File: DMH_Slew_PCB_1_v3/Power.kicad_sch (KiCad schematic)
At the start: 13 parts, among them J0 Conn_01x01, J100 IDC_02x08, J200 IDC_02x05, U10 LM4040LP-10, U11 LM4040LP-10

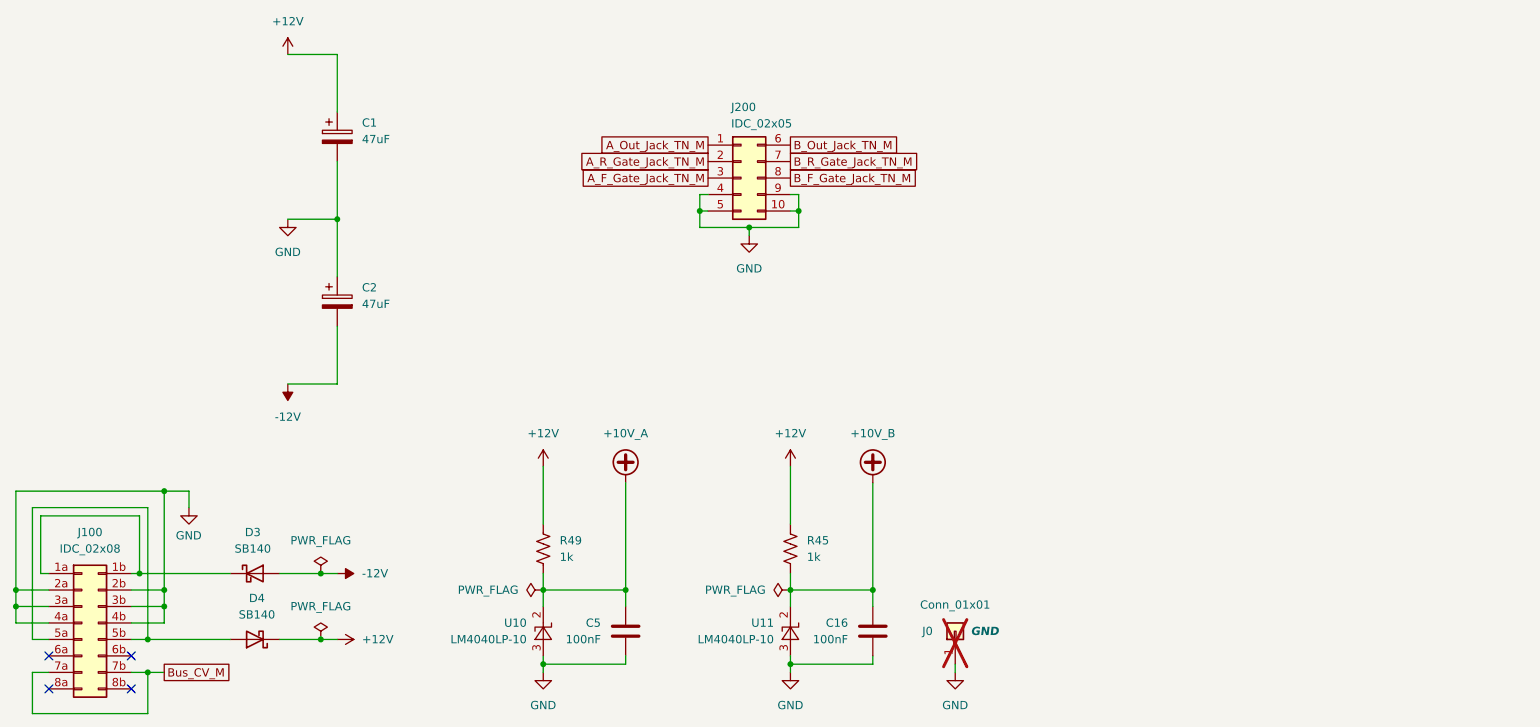
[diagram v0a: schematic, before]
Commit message: Redesigned Main PCB
and regenerated Gerbers
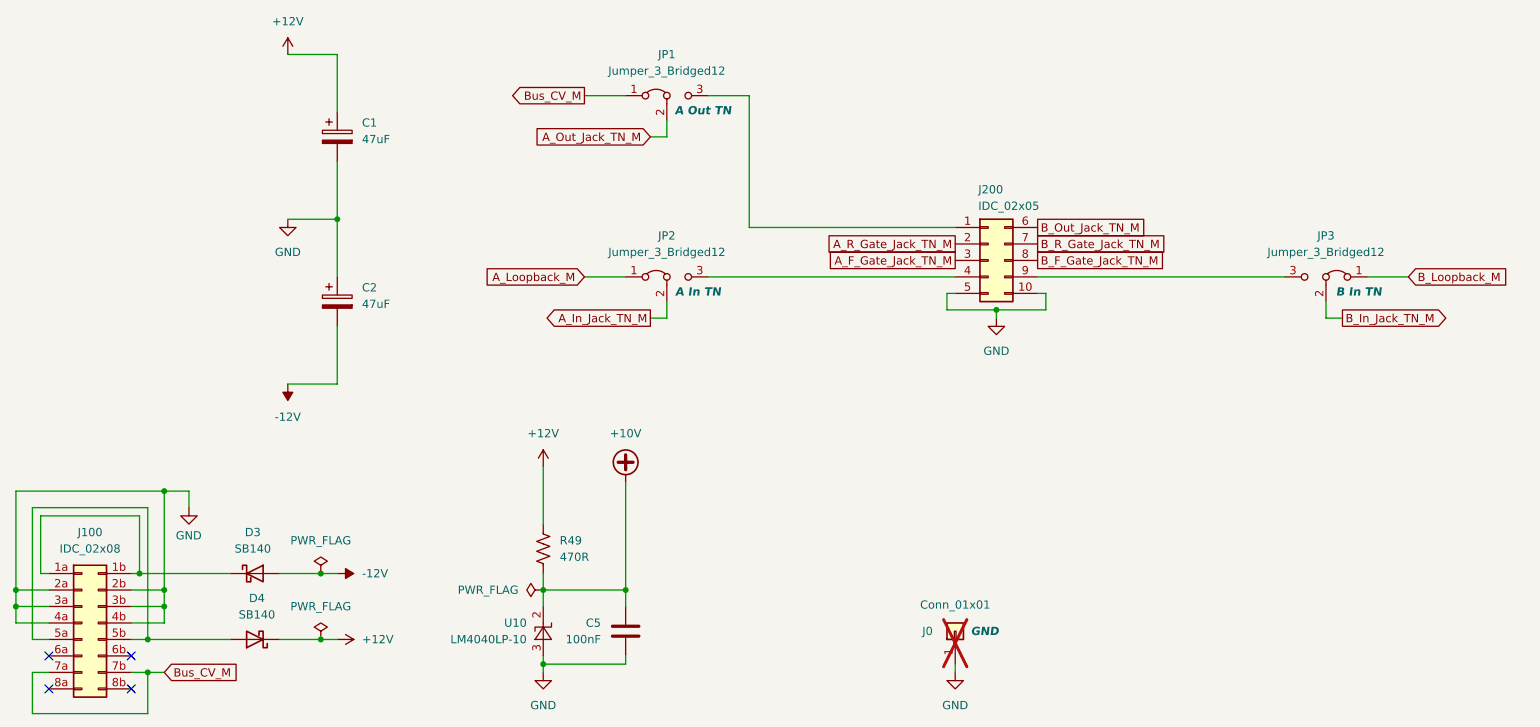
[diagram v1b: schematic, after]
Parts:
- removed C16: 100nF, Capacitor_THT:C_Disc_D4.3mm_W1.9mm_P5.00mm, symbol Device:C
- removed R45: 1k, Resistor_THT:R_Axial_DIN0207_L6.3mm_D2.5mm_P7.62mm_Horizontal, symbol Device:R_US
- removed U11: LM4040LP-10, Package_TO_SOT_THT:TO-92_Inline, symbol Reference_Voltage:LM4040LP-10
- added JP1, JP2, JP3: Jumper_3_Bridged12, Connector_PinHeader_2.54mm:PinHeader_1x03_P2.54mm_Vertical, symbol Jumper:Jumper_3_Bridged12
- R49: value 1k -> 470R
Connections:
- net A_Out_Jack_TN_M: now also JP1.2 (C); no longer J200.1 (Pin_1)
- net Bus_CV_M: now also JP1.1 (A)
- net GND: no longer J200.4 (Pin_4), J200.9 (Pin_9)
- net +10V_A renamed +10V
- new net: J200.1 (Pin_1), JP1.3 (B)
- new net: J200.4 (Pin_4), JP2.3 (B)
- new net: J200.9 (Pin_9), JP3.3 (B)
- new net A_In_Jack_TN_M: JP2.2 (C)
- new net A_Loopback_M: JP2.1 (A)
- new net B_In_Jack_TN_M: JP3.2 (C)
- new net B_Loopback_M: JP3.1 (A)
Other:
- moved on the sheet: J200
